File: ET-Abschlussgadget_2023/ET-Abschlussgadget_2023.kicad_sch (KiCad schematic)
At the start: 13 parts, among them U1 ATtiny10-TS

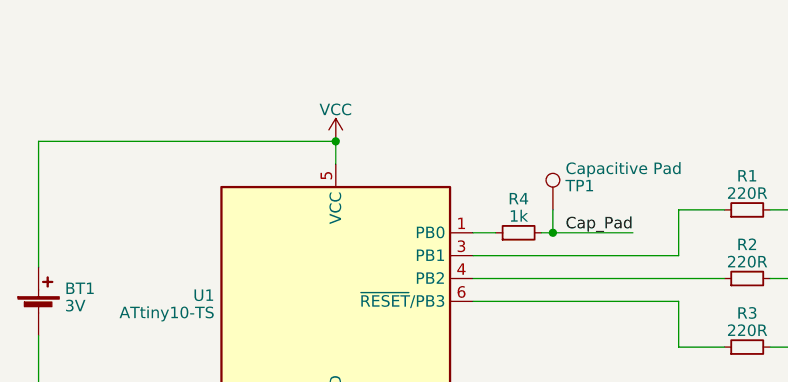
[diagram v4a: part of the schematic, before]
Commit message: Add bypass capacitor
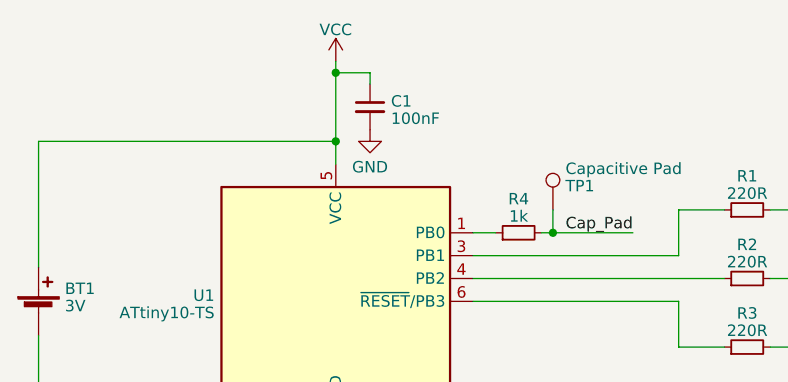
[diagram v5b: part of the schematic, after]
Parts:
- added C1: 100nF, Capacitor_SMD:C_0805_2012Metric_Pad1.18x1.45mm_HandSolder, symbol Device:C_Small
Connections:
- net GND: now also C1.2
- net VCC: now also C1.1
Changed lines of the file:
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@@
   (junction (at 88.9 71.12) (diameter 0) (color 0 0 0 0)
   )
+  (junction (at 88.9 63.5) (diameter 0) (color 0 0 0 0)
+  )
   (junction (at 142.24 78.74) (diameter 0) (color 0 0 0 0)
   )
@@
     (stroke (width 0) (type default))
   )
+  (wire (pts (xy 88.9 63.5) (xy 88.9 71.12))
+    (stroke (width 0) (type default))
+  )
   (wire (pts (xy 170.18 93.98) (xy 156.21 93.98))
     (stroke (width 0) (type default))
@@
     (stroke (width 0) (type default))
   )
+  (wire (pts (xy 88.9 62.23) (xy 88.9 63.5))
+    (stroke (width 0) (type default))
+  )
   (wire (pts (xy 142.24 86.36) (xy 156.21 86.36))
     (stroke (width 0) (type default))
@@
     (stroke (width 0) (type default))
   )
+  (wire (pts (xy 92.71 63.5) (xy 88.9 63.5))
+    (stroke (width 0) (type default))
+  )
   (wire (pts (xy 55.88 71.12) (xy 88.9 71.12))
     (stroke (width 0) (type default))
@@
   )
   (wire (pts (xy 142.24 78.74) (xy 137.16 78.74))
+    (stroke (width 0) (type default))
+  )
+  (wire (pts (xy 92.71 64.77) (xy 92.71 63.5))
     (stroke (width 0) (type default))
   )
@@
     )
   )
-  (symbol (lib_id "power:VCC") (at 88.9 71.12 0) (unit 1)
-    (in_bom yes) (on_board yes) (dnp no) (fields_autoplaced)
-    (property "Reference" "#PWR01" (at 88.9 74.93 0)
-      (effects (font (size 1.27 1.27)) hide)
-    )
-    (property "Value" "VCC" (at 88.9 67.6181 0)
-      (effects (font (size 1.27 1.27)))
-    )
-    (property "Footprint" "" (at 88.9 71.12 0)
-      (effects (font (size 1.27 1.27)) hide)
-    )
-    (property "Datasheet" "" (at 88.9 71.12 0)
+  (symbol (lib_id "power:VCC") (at 88.9 62.23 0) (unit 1)
+    (in_bom yes) (on_board yes) (dnp no) (fields_autoplaced)
+    (property "Reference" "#PWR01" (at 88.9 66.04 0)
+      (effects (font (size 1.27 1.27)) hide)
+    )
+    (property "Value" "VCC" (at 88.9 58.7281 0)
+      (effects (font (size 1.27 1.27)))
+    )
+    (property "Footprint" "" (at 88.9 62.23 0)
+      (effects (font (size 1.27 1.27)) hide)
+    )
+    (property "Datasheet" "" (at 88.9 62.23 0)
       (effects (font (size 1.27 1.27)) hide)
     )
@@
         )
       )
+    )
+  )
+  (symbol (lib_id "power:GND") (at 92.71 69.85 0) (unit 1)
+    (in_bom yes) (on_board yes) (dnp no) (fields_autoplaced)
+    (property "Reference" "#PWR03" (at 92.71 76.2 0)
+      (effects (font (size 1.27 1.27)) hide)
+    )
+    (property "Value" "GND" (at 92.71 73.9855 0)
+      (effects (font (size 1.27 1.27)))
+    )
+    (property "Footprint" "" (at 92.71 69.85 0)
+      (effects (font (size 1.27 1.27)) hide)
+    )
+    (property "Datasheet" "" (at 92.71 69.85 0)
+      (effects (font (size 1.27 1.27)) hide)
+    )
+    (pin "1")
+    (instances
+      (project "ET-Abschlussgadget_2023"
+        (path "/175a65ba-6b59-4269-bd86-2662d331b61e"
+          (reference "#PWR03") (unit 1)
+        )
+      )
+    )
+  )
+  (symbol (lib_id "Device:C_Small") (at 92.71 67.31 0) (unit 1)
+    (in_bom yes) (on_board yes) (dnp no) (fields_autoplaced)
+    (property "Reference" "C1" (at 95.0341 66.6726 0)
+      (effects (font (size 1.27 1.27)) (justify left))
+    )
+    (property "Value" "100nF" (at 95.0341 68.5936 0)
+      (effects (font (size 1.27 1.27)) (justify left))
+    )
+    (property "Footprint" "Capacitor_SMD:C_0805_2012Metric_Pad1.18x1.45mm_HandSolder" (at 92.71 67.31 0)
+      (effects (font (size 1.27 1.27)) hide)
+    )
+    (property "Datasheet" "~" (at 92.71 67.31 0)
+      (effects (font (size 1.27 1.27)) hide)
+    )
+    (pin "1")
+    (pin "2")
+    (instances
+      (project "ET-Abschlussgadget_2023"
+        (path "/175a65ba-6b59-4269-bd86-2662d331b61e"
+          (reference "C1") (unit 1)
+        )
+      )

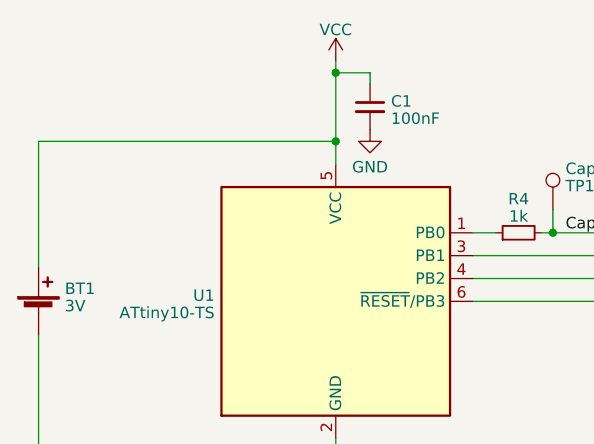
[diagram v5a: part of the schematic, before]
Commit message: Add switch, Change qr to be smaller
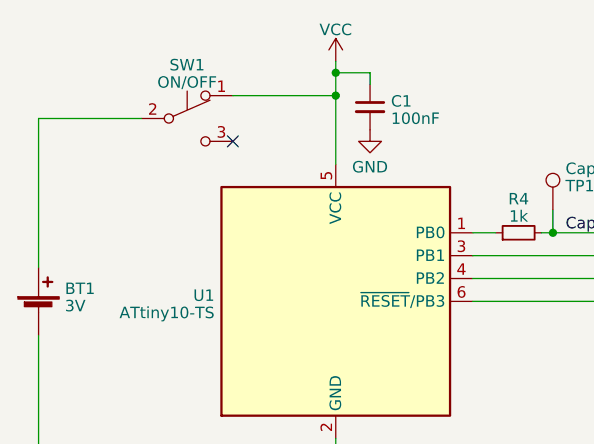
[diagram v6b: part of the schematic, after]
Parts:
- added SW1: ON/OFF, Button_Switch_SMD:SW_SPDT_PCM12, symbol Switch:SW_Push_SPDT
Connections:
- net VCC: now also SW1.1 (A); no longer BT1.1 (+)
- new net: BT1.1 (+), SW1.2 (B)
- no-connect marks 0 -> 1
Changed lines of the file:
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@@
   (junction (at 170.18 93.98) (diameter 0) (color 0 0 0 0)
-  )
-  (junction (at 88.9 71.12) (diameter 0) (color 0 0 0 0)
   )
   (junction (at 88.9 63.5) (diameter 0) (color 0 0 0 0)
@@
   (junction (at 156.21 78.74) (diameter 0) (color 0 0 0 0)
   )
-  (wire (pts (xy 55.88 85.09) (xy 55.88 71.12))
+  (junction (at 88.9 66.04) (diameter 0) (color 0 0 0 0)
+  )
+  (no_connect (at 77.47 71.12))
+  (wire (pts (xy 55.88 68.58) (xy 55.88 85.09))
     (stroke (width 0) (type default))
   )
@@
     (stroke (width 0) (type default))
   )
-  (wire (pts (xy 88.9 63.5) (xy 88.9 71.12))
+  (wire (pts (xy 77.47 66.04) (xy 88.9 66.04))
     (stroke (width 0) (type default))
   )
@@
   )
   (wire (pts (xy 113.03 81.28) (xy 121.92 81.28))
+    (stroke (width 0) (type default))
+  )
+  (wire (pts (xy 88.9 63.5) (xy 88.9 66.04))
     (stroke (width 0) (type default))
   )
@@
   )
   (wire (pts (xy 104.14 88.9) (xy 127 88.9))
-    (stroke (width 0) (type default))
-  )
-  (wire (pts (xy 88.9 71.12) (xy 88.9 73.66))
     (stroke (width 0) (type default))
   )
@@
     (stroke (width 0) (type default))
   )
-  (wire (pts (xy 55.88 71.12) (xy 88.9 71.12))
+  (wire (pts (xy 182.88 83.82) (xy 182.88 78.74))
     (stroke (width 0) (type default))
   )
-  (wire (pts (xy 182.88 83.82) (xy 182.88 78.74))
+  (wire (pts (xy 88.9 66.04) (xy 88.9 73.66))
     (stroke (width 0) (type default))
   )
@@
     (stroke (width 0) (type default))
   )
+  (wire (pts (xy 55.88 68.58) (xy 67.31 68.58))
+    (stroke (width 0) (type default))
+  )
   (wire (pts (xy 156.21 86.36) (xy 156.21 87.63))
     (stroke (width 0) (type default))
@@
     (effects (font (size 1.27 1.27)) (justify right bottom))
   )
+  (symbol (lib_id "Switch:SW_Push_SPDT") (at 72.39 68.58 0) (unit 1)
+    (in_bom yes) (on_board yes) (dnp no)
+    (property "Reference" "SW1" (at 72.39 62.6491 0)
+      (effects (font (size 1.27 1.27)))
+    )
+    (property "Value" "ON/OFF" (at 72.39 64.5701 0)
+      (effects (font (size 1.27 1.27)))
+    )
+    (property "Footprint" "Button_Switch_SMD:SW_SPDT_PCM12" (at 72.39 68.58 0)
+      (effects (font (size 1.27 1.27)) hide)
+    )
+    (property "Datasheet" "~" (at 72.39 68.58 0)
+      (effects (font (size 1.27 1.27)) hide)
+    )
+    (pin "1")
+    (pin "2")
+    (pin "3")
+    (instances
+      (project "ET-Abschlussgadget_2023"
+        (path "/175a65ba-6b59-4269-bd86-2662d331b61e"
+          (reference "SW1") (unit 1)
+        )
+      )
+    )
+  )
   (symbol (lib_id "Device:LED_Small") (at 142.24 82.55 270) (unit 1)

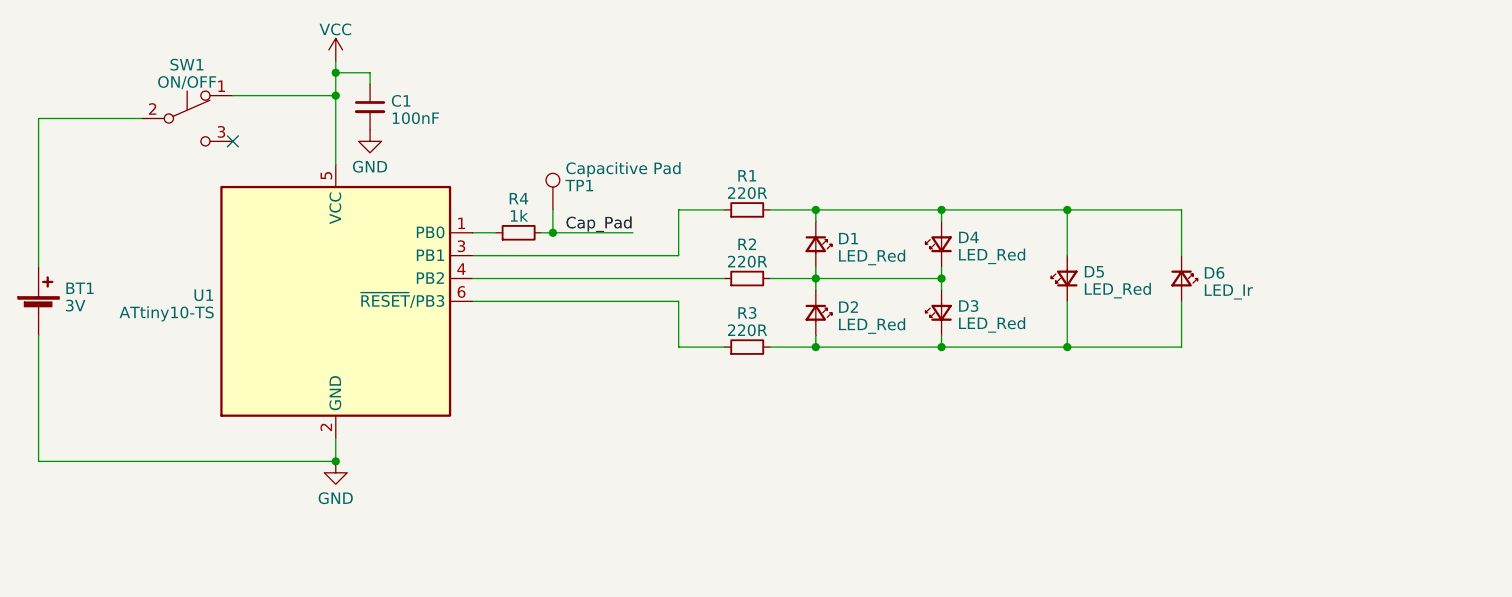
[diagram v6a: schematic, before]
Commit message: Add material-list, Adjust footprints, add first datasheets
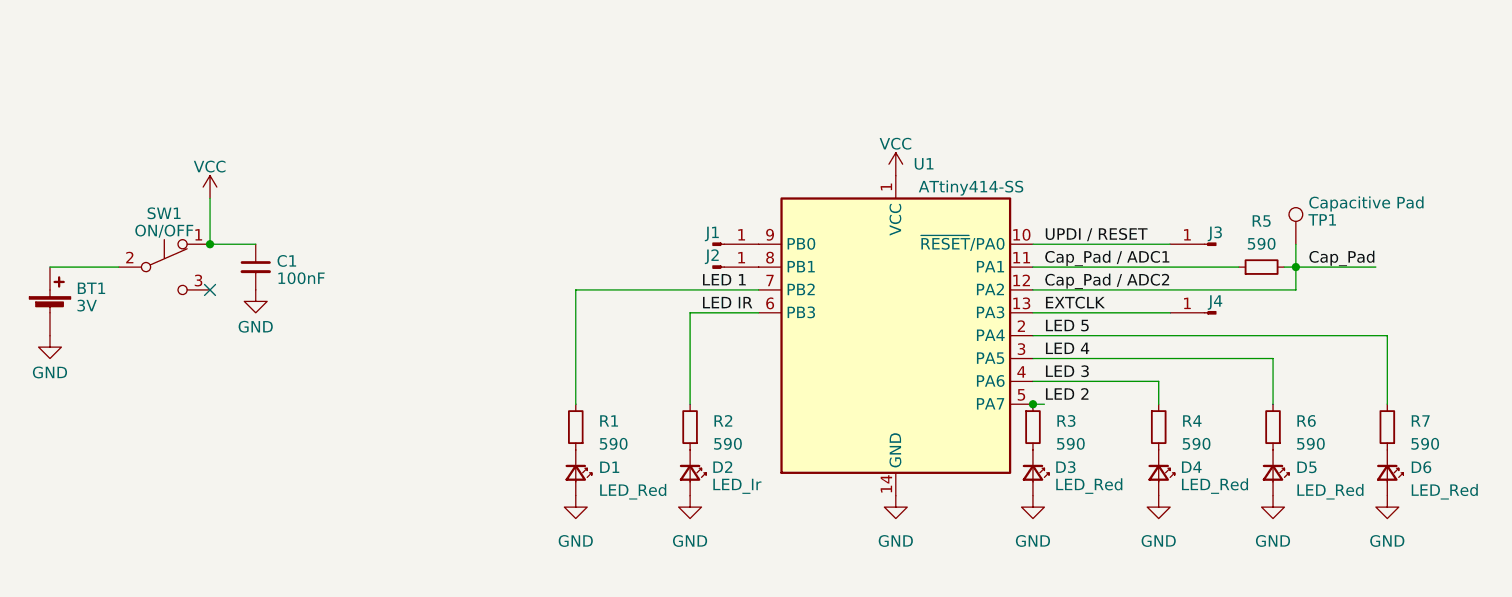
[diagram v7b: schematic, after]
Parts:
- removed U1: ATtiny10-TS, Package_TO_SOT_SMD:SOT-23-6, symbol MCU_Microchip_ATtiny:ATtiny10-TS
- added J1: PB0, TestPoint:TestPoint_Pad_D1.0mm, symbol Connector:Conn_01x01_Pin
- added J2: PB1, TestPoint:TestPoint_Pad_D1.0mm, symbol Connector:Conn_01x01_Pin
- added J3: UPDI / RESET, TestPoint:TestPoint_Pad_D2.0mm, symbol Connector:Conn_01x01_Pin
- added J4: EXTCLK, TestPoint:TestPoint_Pad_D2.0mm, symbol Connector:Conn_01x01_Pin
- added R1, R2, R7: 590, Resistor_SMD:R_0805_2012Metric_Pad1.20x1.40mm_HandSolder, symbol Device:R_Small
- added U1: ATtiny414-SS, Package_SO:SOIC-14_3.9x8.7mm_P1.27mm, symbol MCU_Microchip_ATtiny:ATtiny414-SS
- BT1: footprint Battery:BatteryHolder_Keystone_3000_1x12mm -> Battery:BatteryHolder_Keystone_3002_1x2032
- D1: renamed from D5; footprint LED_SMD:LED_0805_2012Metric_Pad1.15x1.40mm_HandSolder -> LED_SMD:LED_0603_1608Metric
- D2: renamed from D6; footprint LED_SMD:LED_LiteOn_LTST-S326 -> LED_SMD:LED_1206_3216Metric
- D3: renamed from D1; footprint LED_SMD:LED_0805_2012Metric_Pad1.15x1.40mm_HandSolder -> LED_SMD:LED_0603_1608Metric
- D4: renamed from D2; footprint LED_SMD:LED_0805_2012Metric_Pad1.15x1.40mm_HandSolder -> LED_SMD:LED_0603_1608Metric
- D5: renamed from D3; footprint LED_SMD:LED_0805_2012Metric_Pad1.15x1.40mm_HandSolder -> LED_SMD:LED_0603_1608Metric
- D6: renamed from D4; footprint LED_SMD:LED_0805_2012Metric_Pad1.15x1.40mm_HandSolder -> LED_SMD:LED_0603_1608Metric
- R3: renamed from R1; value 220R -> 590
- R4: renamed from R2; value 220R -> 590
- R5: renamed from R4; value 1k -> 590
- R6: renamed from R3; value 220R -> 590
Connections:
- net Cap_Pad: now also U1.12 (PA2)
- net GND: now also D1.2 (A), D2.2 (A), D3.2 (A), D4.2 (A), D5.2 (A), D6.2 (A), U1.14 (GND)
- net VCC: now also U1.1 (VCC)
- net at R6.1: now also D5.1 (K)
- net Cap_Pad / ADC1: now reaches R5.1
- net Cap_Pad / ADC1: now also U1.11 (PA1)
- net LED 3: now reaches R4.1
- net LED 3: now also U1.4 (PA6)
- net LED 2: now reaches R3.1
- net LED 2: now also U1.5 (PA7)
- new net: D3.1 (K), R3.2
- new net: J2.1 (Pin_1), U1.8 (PB1)
- new net: D6.1 (K), R7.1
- new net: D1.1 (K), R1.1
- new net: D2.1 (K), R2.1
- new net: J1.1 (Pin_1), U1.9 (PB0)
- new net: D4.1 (K), R4.2
- new net EXTCLK: J4.1 (Pin_1), U1.13 (PA3)
- new net LED 1: R1.2, U1.7 (PB2)
- new net LED 4: R6.2, U1.3 (PA5)
- new net LED 5: R7.2, U1.2 (PA4)
- new net LED IR: R2.2, U1.6 (PB3)
- new net UPDI / RESET: J3.1 (Pin_1), U1.10 (~{RESET}/PA0)
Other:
- moved on the sheet: D1, D2, D3, D4, D5, D6, R3, R4, R5, R6, TP1
